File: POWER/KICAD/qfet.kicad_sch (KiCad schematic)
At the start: 5 parts

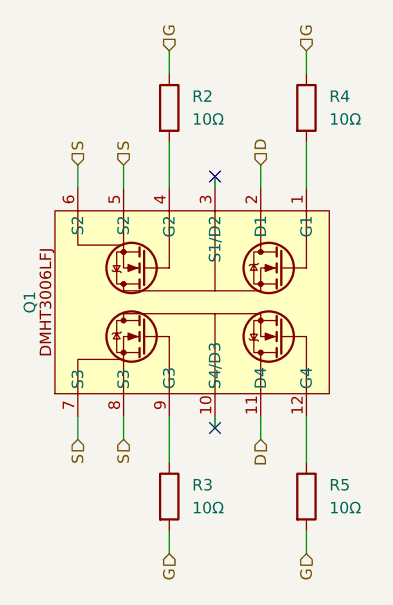
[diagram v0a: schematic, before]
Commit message: Edited Schematics
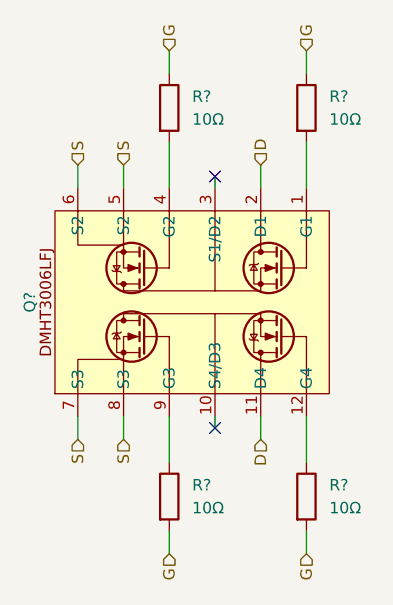
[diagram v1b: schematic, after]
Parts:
- renumbered Q1 to Q?, R5 to R?, R4 to R?, R3 to R?, R2 to R?
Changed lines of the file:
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@@
 		(dnp no)
 		(fields_autoplaced yes)
-		(property "Reference" "R5"
+		(property "Reference" "R?"
 			(at 154.94 114.2999 0)
 			(effects
@@
 			(project "control"
 				(path "/c4b3c8f9-82bd-4648-8d22-870bf16aa829/8812c96e-ca04-41e1-abbd-8267da6f4a17/4f67d7e5-b4f1-4280-8ca9-89c489da0499/b44fa901-dbbb-4255-9c8a-45abddcd36be"
-					(reference "R5")
+					(reference "R?")
 					(unit 1)
 				)
@@
 		(dnp no)
 		(fields_autoplaced yes)
-		(property "Reference" "R4"
+		(property "Reference" "R?"
 			(at 154.94 71.1199 0)
 			(effects
@@
 			(project "control"
 				(path "/c4b3c8f9-82bd-4648-8d22-870bf16aa829/8812c96e-ca04-41e1-abbd-8267da6f4a17/4f67d7e5-b4f1-4280-8ca9-89c489da0499/b44fa901-dbbb-4255-9c8a-45abddcd36be"
-					(reference "R4")
+					(reference "R?")
 					(unit 1)
 				)
@@
 		(dnp no)
 		(fields_autoplaced yes)
-		(property "Reference" "Q1"
+		(property "Reference" "Q?"
 			(at 121.666 93.98 0)
 			(do_not_autoplace yes)
@@
 			(project "control"
 				(path "/c4b3c8f9-82bd-4648-8d22-870bf16aa829/8812c96e-ca04-41e1-abbd-8267da6f4a17/4f67d7e5-b4f1-4280-8ca9-89c489da0499/b44fa901-dbbb-4255-9c8a-45abddcd36be"
-					(reference "Q1")
+					(reference "Q?")
 					(unit 1)
 				)
@@
 		(dnp no)
 		(fields_autoplaced yes)
-		(property "Reference" "R3"
+		(property "Reference" "R?"
 			(at 139.7 114.2999 0)
 			(effects
@@
 			(project "control"
 				(path "/c4b3c8f9-82bd-4648-8d22-870bf16aa829/8812c96e-ca04-41e1-abbd-8267da6f4a17/4f67d7e5-b4f1-4280-8ca9-89c489da0499/b44fa901-dbbb-4255-9c8a-45abddcd36be"
-					(reference "R3")
+					(reference "R?")
 					(unit 1)
 				)
@@
 		(dnp no)
 		(fields_autoplaced yes)
-		(property "Reference" "R2"
+		(property "Reference" "R?"
 			(at 139.7 71.1199 0)
 			(effects
@@
 			(project "control"
 				(path "/c4b3c8f9-82bd-4648-8d22-870bf16aa829/8812c96e-ca04-41e1-abbd-8267da6f4a17/4f67d7e5-b4f1-4280-8ca9-89c489da0499/b44fa901-dbbb-4255-9c8a-45abddcd36be"
-					(reference "R2")
-					(unit 1)
-				)
+					(reference "R?")
+					(unit 1)
+				)

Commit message: Updated Power Schematic / Kicad
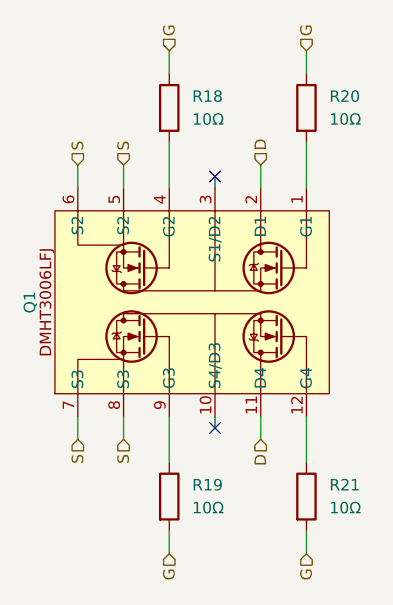
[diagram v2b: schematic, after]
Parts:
- gave numbers to parts that had none: 5
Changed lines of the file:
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@@
 		(dnp no)
 		(fields_autoplaced yes)
-		(property "Reference" "R?"
+		(property "Reference" "R21"
 			(at 154.94 114.2999 0)
 			(effects
@@
 			(project "control"
 				(path "/c4b3c8f9-82bd-4648-8d22-870bf16aa829/8812c96e-ca04-41e1-abbd-8267da6f4a17/4f67d7e5-b4f1-4280-8ca9-89c489da0499/b44fa901-dbbb-4255-9c8a-45abddcd36be"
-					(reference "R?")
+					(reference "R21")
 					(unit 1)
 				)
@@
 			(project "command"
 				(path "/e00fbfc6-dde6-474b-a191-76d0397e7dbb/fc69eaab-145a-4b23-932e-6f5d1f636f2f/b44fa901-dbbb-4255-9c8a-45abddcd36be"
+					(reference "R?")
+					(unit 1)
+				)
+			)
+			(project "power"
+				(path "/ef47adc1-536f-4520-9ebd-fa1d01e89711/2e64aba1-9872-4229-a91b-1ccd7b04c751/b44fa901-dbbb-4255-9c8a-45abddcd36be"
 					(reference "R?")
 					(unit 1)
@@
 		(dnp no)
 		(fields_autoplaced yes)
-		(property "Reference" "R?"
+		(property "Reference" "R20"
 			(at 154.94 71.1199 0)
 			(effects
@@
 			(project "control"
 				(path "/c4b3c8f9-82bd-4648-8d22-870bf16aa829/8812c96e-ca04-41e1-abbd-8267da6f4a17/4f67d7e5-b4f1-4280-8ca9-89c489da0499/b44fa901-dbbb-4255-9c8a-45abddcd36be"
-					(reference "R?")
+					(reference "R20")
 					(unit 1)
 				)
@@
 			(project "command"
 				(path "/e00fbfc6-dde6-474b-a191-76d0397e7dbb/fc69eaab-145a-4b23-932e-6f5d1f636f2f/b44fa901-dbbb-4255-9c8a-45abddcd36be"
+					(reference "R?")
+					(unit 1)
+				)
+			)
+			(project "power"
+				(path "/ef47adc1-536f-4520-9ebd-fa1d01e89711/2e64aba1-9872-4229-a91b-1ccd7b04c751/b44fa901-dbbb-4255-9c8a-45abddcd36be"
 					(reference "R?")
 					(unit 1)
@@
 		(dnp no)
 		(fields_autoplaced yes)
-		(property "Reference" "Q?"
+		(property "Reference" "Q1"
 			(at 121.666 93.98 0)
 			(do_not_autoplace yes)
@@
 			(project "control"
 				(path "/c4b3c8f9-82bd-4648-8d22-870bf16aa829/8812c96e-ca04-41e1-abbd-8267da6f4a17/4f67d7e5-b4f1-4280-8ca9-89c489da0499/b44fa901-dbbb-4255-9c8a-45abddcd36be"
-					(reference "Q?")
+					(reference "Q1")
 					(unit 1)
 				)
@@
 			(project "command"
 				(path "/e00fbfc6-dde6-474b-a191-76d0397e7dbb/fc69eaab-145a-4b23-932e-6f5d1f636f2f/b44fa901-dbbb-4255-9c8a-45abddcd36be"
+					(reference "Q?")
+					(unit 1)
+				)
+			)
+			(project "power"
+				(path "/ef47adc1-536f-4520-9ebd-fa1d01e89711/2e64aba1-9872-4229-a91b-1ccd7b04c751/b44fa901-dbbb-4255-9c8a-45abddcd36be"
 					(reference "Q?")
 					(unit 1)
@@
 		(dnp no)
 		(fields_autoplaced yes)
-		(property "Reference" "R?"
+		(property "Reference" "R19"
 			(at 139.7 114.2999 0)
 			(effects
@@
 			(project "control"
 				(path "/c4b3c8f9-82bd-4648-8d22-870bf16aa829/8812c96e-ca04-41e1-abbd-8267da6f4a17/4f67d7e5-b4f1-4280-8ca9-89c489da0499/b44fa901-dbbb-4255-9c8a-45abddcd36be"
-					(reference "R?")
+					(reference "R19")
 					(unit 1)
 				)
@@
 			(project "command"
 				(path "/e00fbfc6-dde6-474b-a191-76d0397e7dbb/fc69eaab-145a-4b23-932e-6f5d1f636f2f/b44fa901-dbbb-4255-9c8a-45abddcd36be"
+					(reference "R?")
+					(unit 1)
+				)
+			)
+			(project "power"
+				(path "/ef47adc1-536f-4520-9ebd-fa1d01e89711/2e64aba1-9872-4229-a91b-1ccd7b04c751/b44fa901-dbbb-4255-9c8a-45abddcd36be"
 					(reference "R?")
 					(unit 1)
@@
 		(dnp no)
 		(fields_autoplaced yes)
-		(property "Reference" "R?"
+		(property "Reference" "R18"
 			(at 139.7 71.1199 0)
 			(effects
@@
 			(project "control"
 				(path "/c4b3c8f9-82bd-4648-8d22-870bf16aa829/8812c96e-ca04-41e1-abbd-8267da6f4a17/4f67d7e5-b4f1-4280-8ca9-89c489da0499/b44fa901-dbbb-4255-9c8a-45abddcd36be"
-					(reference "R?")
+					(reference "R18")
 					(unit 1)
 				)
@@
 					(reference "R?")
 					(unit 1)
+				)
+			)
+			(project "power"
+				(path "/ef47adc1-536f-4520-9ebd-fa1d01e89711/2e64aba1-9872-4229-a91b-1ccd7b04c751/b44fa901-dbbb-4255-9c8a-45abddcd36be"
+					(reference "R?")
+					(unit 1)
